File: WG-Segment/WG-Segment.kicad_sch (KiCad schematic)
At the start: 1 part, among them J1 Conn_02x04_Odd_Even

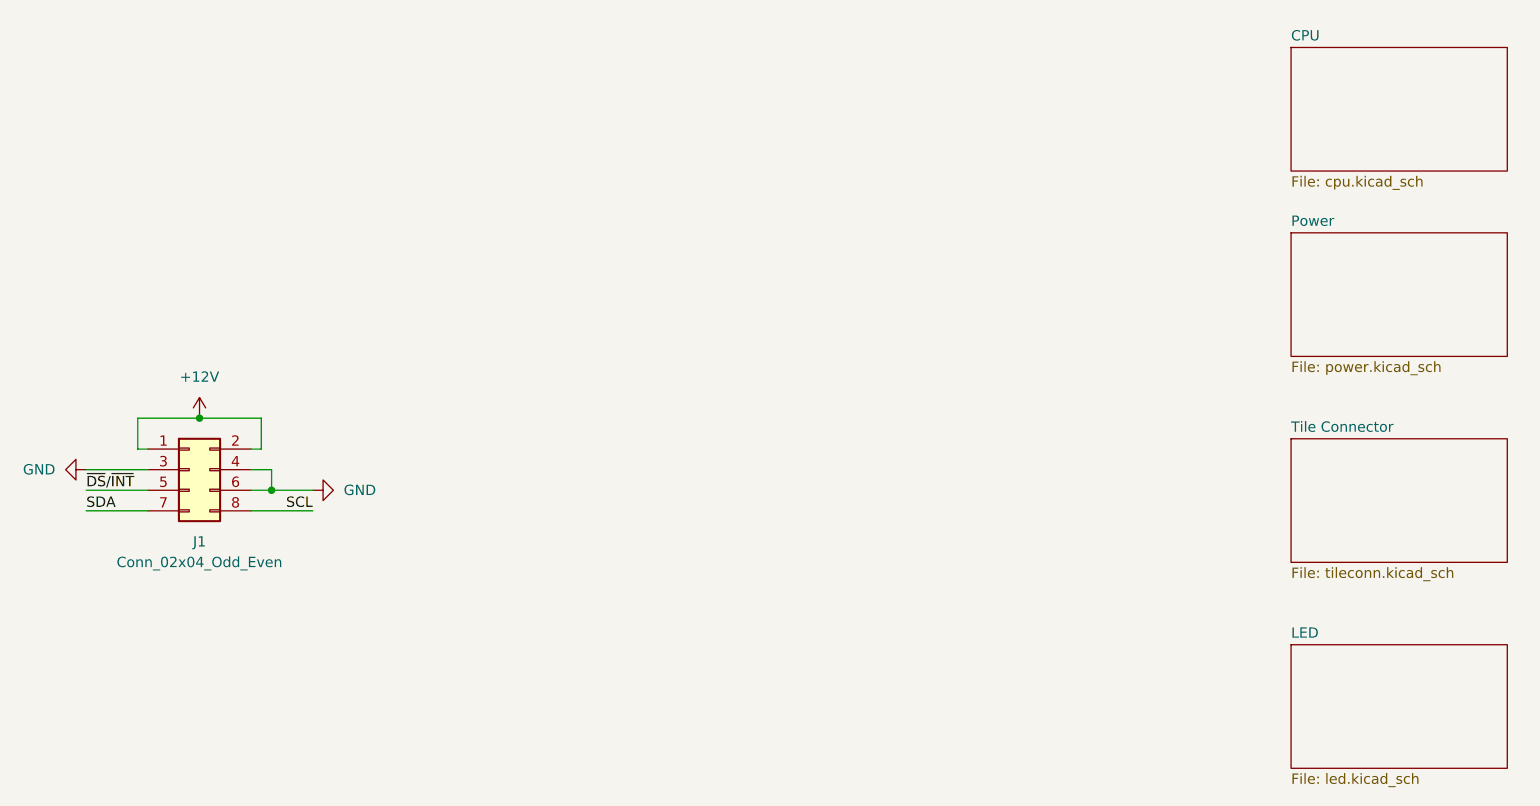
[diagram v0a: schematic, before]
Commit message: Design full circuit
Still need to run ERC
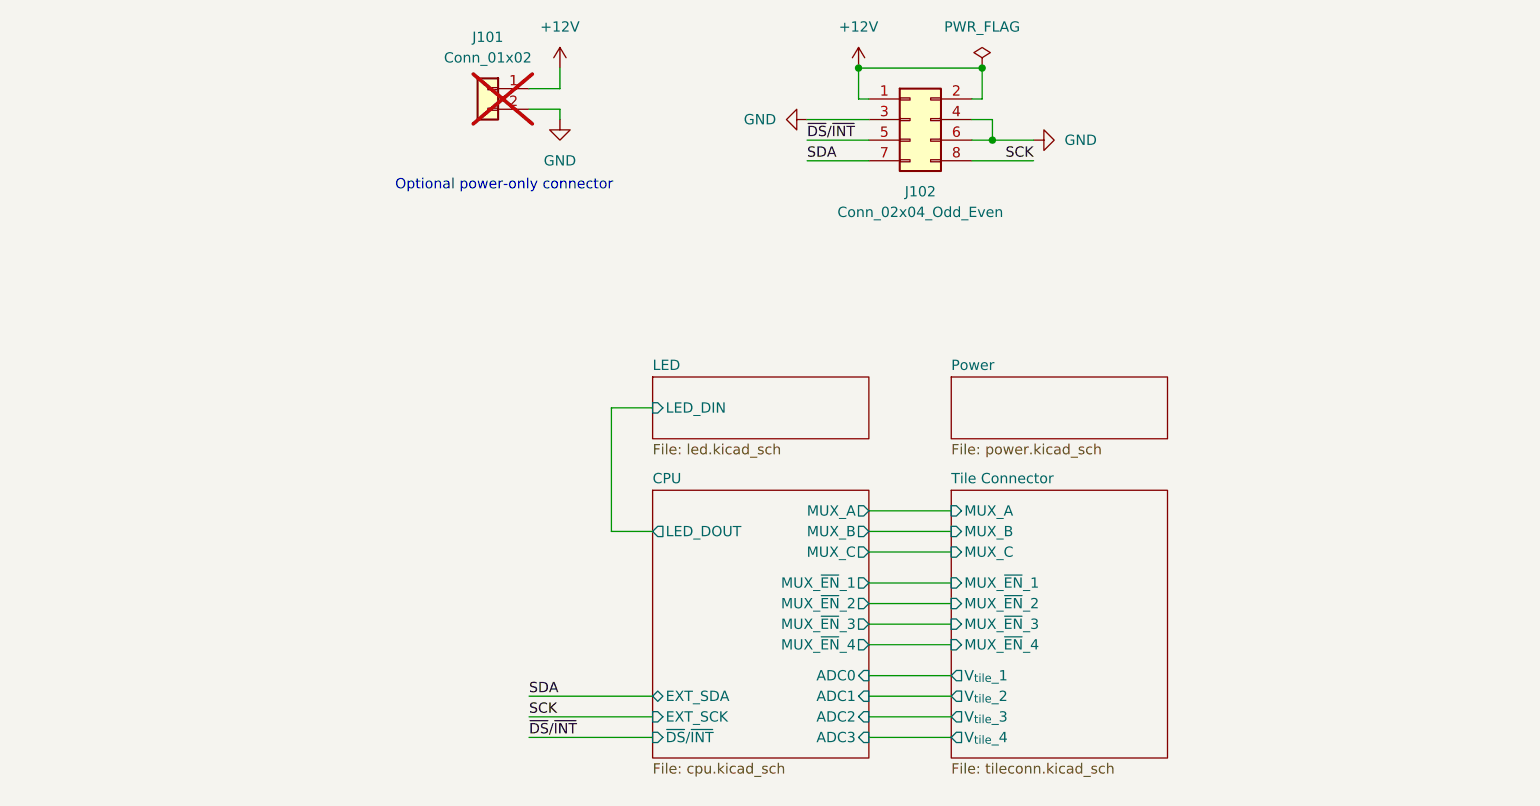
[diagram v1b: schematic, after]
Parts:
- added J101: Conn_01x02, Connector_Wire:SolderWire-0.5sqmm_1x02_P4.6mm_D0.9mm_OD2.1mm, symbol Connector_Generic:Conn_01x02
- renumbered J1 to J102
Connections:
- net +12V: now also J101.1 (Pin_1)
- net GND: now also J101.2 (Pin_2)
- net SCL renamed SCK
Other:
- sheet CPU ports: added ADC0, ADC1, ADC2, ADC3, EXT_SCK, EXT_SDA, LED_DOUT, MUX_A, MUX_B, MUX_C, MUX_~{EN}_1, MUX_~{EN}_2, MUX_~{EN}_3, MUX_~{EN}_4, ~{DS}/~{INT}; removed none
- sheet LED ports: added LED_DIN; removed none
- sheet Tile Connector ports: added MUX_A, MUX_B, MUX_C, MUX_~{EN}_1, MUX_~{EN}_2, MUX_~{EN}_3, MUX_~{EN}_4, V_{tile}_1, V_{tile}_2, V_{tile}_3, V_{tile}_4; removed none
- note added: "Optional power-only connector"
- moved on the sheet: J102

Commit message: Finish designing most of the PCB
Only need to connect analog traces. May need to make the board a 4-layer PCB
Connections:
- net SCK: now also J102.7 (Pin_7); no longer J102.8 (Pin_8)
- net SDA: now also J102.8 (Pin_8); no longer J102.7 (Pin_7)
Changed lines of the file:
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@@
+    (effects (font (size 1.27 1.27)) (justify left bottom))
+  )
+  (label "SCK" (at 137.16 60.96 0) (fields_autoplaced)
     (effects (font (size 1.27 1.27)) (justify left bottom))
   )
@@
     (effects (font (size 1.27 1.27)) (justify left bottom))
   )
-  (label "SCK" (at 165.1 60.96 180) (fields_autoplaced)
+  (label "SDA" (at 165.1 60.96 180) (fields_autoplaced)
     (effects (font (size 1.27 1.27)) (justify right bottom))
   )
@@
     (effects (font (size 1.27 1.27)) (justify left bottom))
   )
-  (label "SDA" (at 137.16 60.96 0) (fields_autoplaced)
-    (effects (font (size 1.27 1.27)) (justify left bottom))
-  )

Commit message: Update connector
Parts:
- J102: footprint Connector_IDC:IDC-Header_2x04_P2.54mm_Vertical -> Connector_JST:JST_PHD_B8B-PHDSS_2x04_P2.00mm_Vertical; Manufacturer (none) -> BOOMELE(Boom Precision Elec); Part Number (none) -> PHD-2*4A
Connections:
- net GND: now also J102.5 (Pin_5); no longer J102.6 (Pin_6)
- net SCK: now also J102.8 (Pin_8); no longer J102.7 (Pin_7)
- net SDA: now also J102.7 (Pin_7); no longer J102.8 (Pin_8)
- net ~{DS}/~{INT}: now also J102.6 (Pin_6); no longer J102.5 (Pin_5)
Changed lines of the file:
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@@
     )
   )
-  (symbol (lib_id "Connector_Generic:Conn_02x04_Odd_Even") (at 149.86 55.88 0) (unit 1)
+  (symbol (lib_id "Connector_Generic:Conn_02x04_Odd_Even") (at 152.4 55.88 0) (mirror y) (unit 1)
     (in_bom yes) (on_board yes) (dnp no)
     (property "Reference" "J102" (at 151.13 64.77 0)
@@
       (effects (font (size 1.27 1.27)))
     )
-    (property "Footprint" "Connector_IDC:IDC-Header_2x04_P2.54mm_Vertical" (at 149.86 55.88 0)
+    (property "Footprint" "Connector_JST:JST_PHD_B8B-PHDSS_2x04_P2.00mm_Vertical" (at 152.4 55.88 0)
       (effects (font (size 1.27 1.27)) hide)
     )
-    (property "Datasheet" "~" (at 149.86 55.88 0)
+    (property "Datasheet" "https://jlcpcb.com/api/file/downloadByFileSystemAccessId/8588886984102727680" (at 152.4 55.88 0)
       (effects (font (size 1.27 1.27)) hide)
     )
+    (property "Part Number" "PHD-2*4A" (at 152.4 55.88 0)
+      (effects (font (size 1.27 1.27)) hide)
+    )
+    (property "Manufacturer" "BOOMELE(Boom Precision Elec)" (at 152.4 55.88 0)
+      (effects (font (size 1.27 1.27)) hide)
+    )
+    (property "Description" "2x4P 8P 2 PHD 2mm 2mm 4 Phosphor Bronze Plugin,P=2mm Wire To Board Connector ROHS" (at 152.4 55.88 0)
+      (effects (font (size 1.27 1.27)) hide)
+    )

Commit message: Fix build issues
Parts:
- J102: Desc (none) -> 2x4P 8P 2 PHD 2mm 2mm 4 Phosphor Bronze Plugin,P=2mm Wire T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
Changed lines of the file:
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@@
       (effects (font (size 1.27 1.27)) hide)
     )
-    (property "Description" "2x4P 8P 2 PHD 2mm 2mm 4 Phosphor Bronze Plugin,P=2mm Wire To Board Connector ROHS" (at 152.4 55.88 0)
+    (property "Desc" "2x4P 8P 2 PHD 2mm 2mm 4 Phosphor Bronze Plugin,P=2mm Wire To Board Connector ROHS" (at 152.4 55.88 0)
       (effects (font (size 1.27 1.27)) hide)
     )
@@
       (effects (font (size 1.27 1.27)) hide)
     )
-    (property "Description" "" (at 97.79 52.07 0)
-      (effects (font (size 1.27 1.27)) hide)
-    )
